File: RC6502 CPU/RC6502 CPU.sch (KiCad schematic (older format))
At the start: 12 parts, among them J1 CONN_01X39, J2 IRQ OnBus, J3 NMI OnBus, J4 VP GND, U1 WD65C02, X1 CXO_DIP14

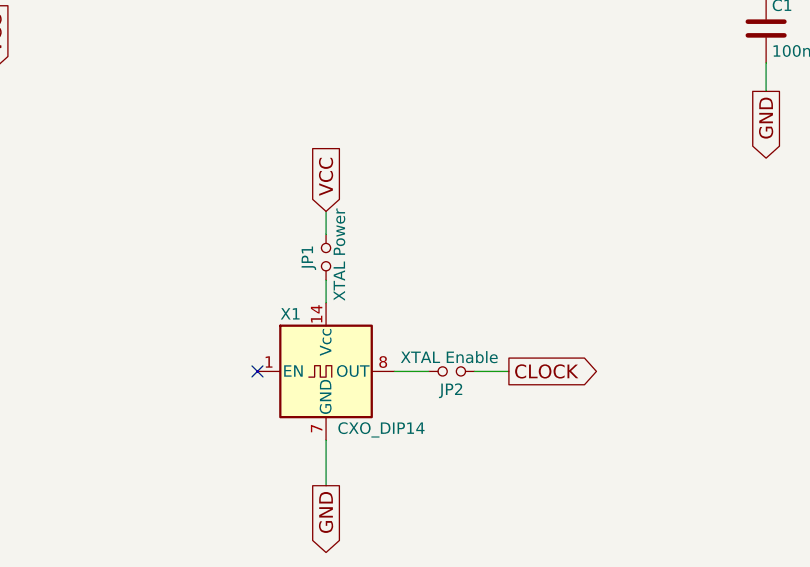
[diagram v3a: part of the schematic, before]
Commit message: CPU revision B
VP pin was added for W65c02, added SYNC and RDY pins and removed hex inverter.
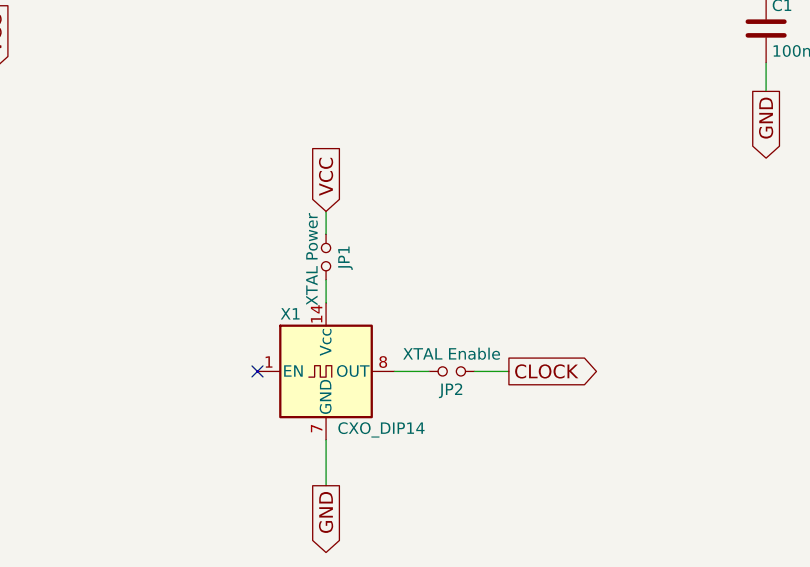
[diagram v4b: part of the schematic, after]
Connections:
- net VCC: now also JP1.1; no longer JP1.2
- net at X1.14 (Vcc): now also JP1.2; no longer JP1.1
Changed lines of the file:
@@
 F 3 "" H 5200 2300 50  0001 C CNN
 	1    5200 2300
-	0    -1   -1   0
+	0    1    1    0
 $EndComp
 Wire Wire Line
@@
 P 5750 2800
 F 0 "JP2" H 5750 2880 50  0000 C CNN
-F 1 "XTAL Enable" H 5760 2740 50  0000 C CNN
+F 1 "XTAL Enable" H 5750 2725 50  0000 C CNN
 F 2 "Pin_Headers:Pin_Header_Angled_1x02_Pitch2.54mm" H 5750 2800 50  0001 C CNN
 F 3 "" H 5750 2800 50  0001 C CNN

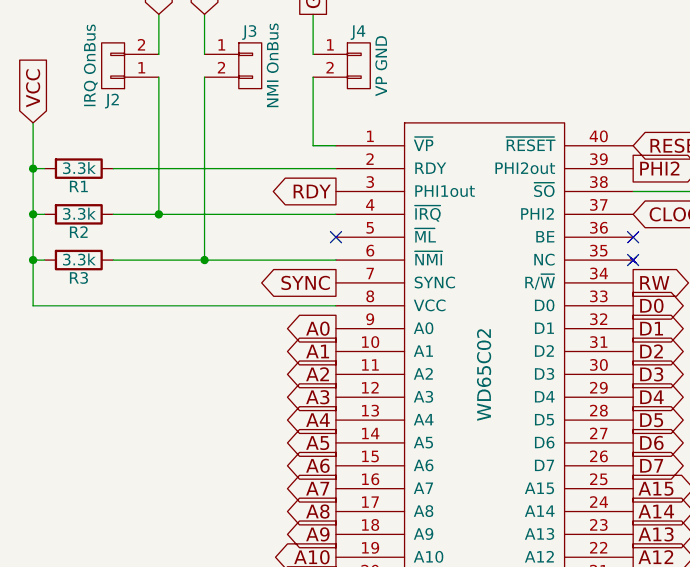
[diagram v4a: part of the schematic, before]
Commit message: Connected RDY to the wrong pin. Ooops!
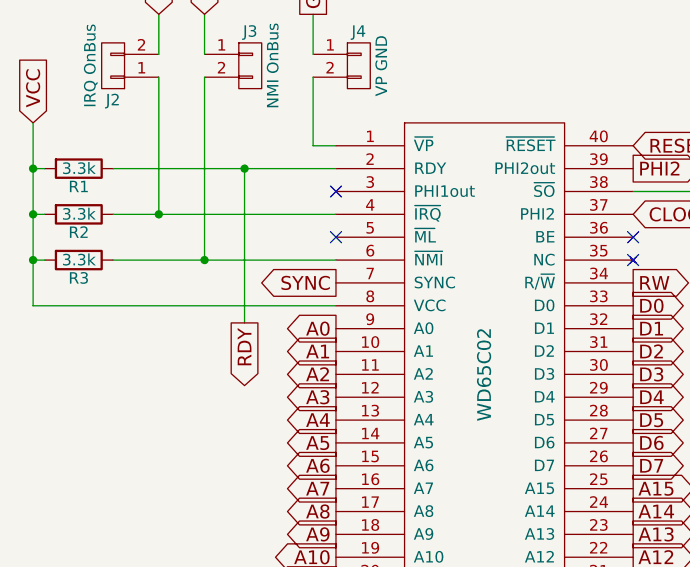
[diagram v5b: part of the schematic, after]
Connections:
- net RDY: now also R1.1, U1.2 (RDY); no longer U1.3 (PHI1out)
- no-connect marks 9 -> 10
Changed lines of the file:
@@
 Text GLabel 9350 4000 0    60   Input ~ 0
 SYNC
-Text GLabel 2000 1800 0    60   Output ~ 0
+Text GLabel 1600 2375 3    60   Output ~ 0
 RDY
 Text GLabel 2000 2200 0    60   Output ~ 0
 SYNC
+Wire Wire Line
+	1600 2375 1600 1700
+Connection ~ 1600 1700
+NoConn ~ 2000 1800
 $EndSCHEMATC
